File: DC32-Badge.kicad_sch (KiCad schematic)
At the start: 43 parts, among them J1 Conn_01x06, J2 Hirose_FH34-SRJ-24S, J3 Conn_01x06, J4 Conn_01x06, J5 Conn_01x06, J5 Micro_SD_Card_Det, P1 2479, Q1 RTF025N03TL, SW1 SW_Push_DPDT, SW2 EVIL_SWITCH, SW3 SW_Push, SW4 SW_Push, SW5 PROGRAM, U1 ESP32-S3-WROOM-1, U2 AP2112K-3.3

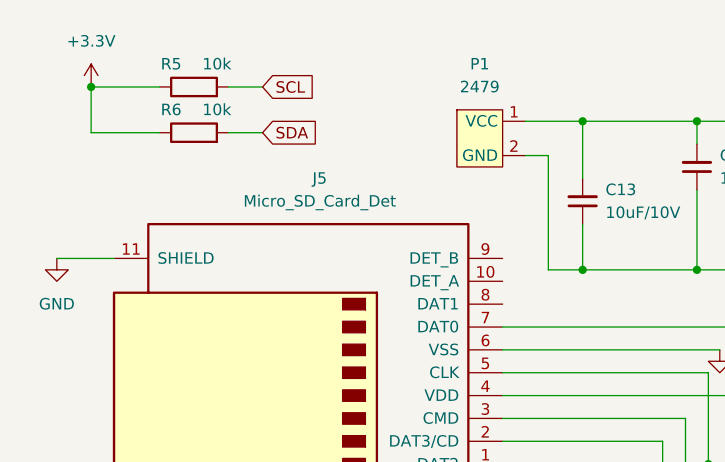
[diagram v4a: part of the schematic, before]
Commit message: Ran electrical rules checker.
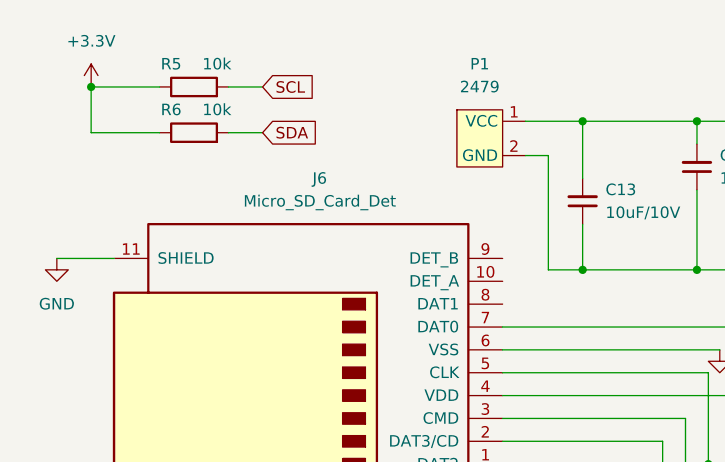
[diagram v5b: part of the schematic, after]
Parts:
- renumbered J5 to J6

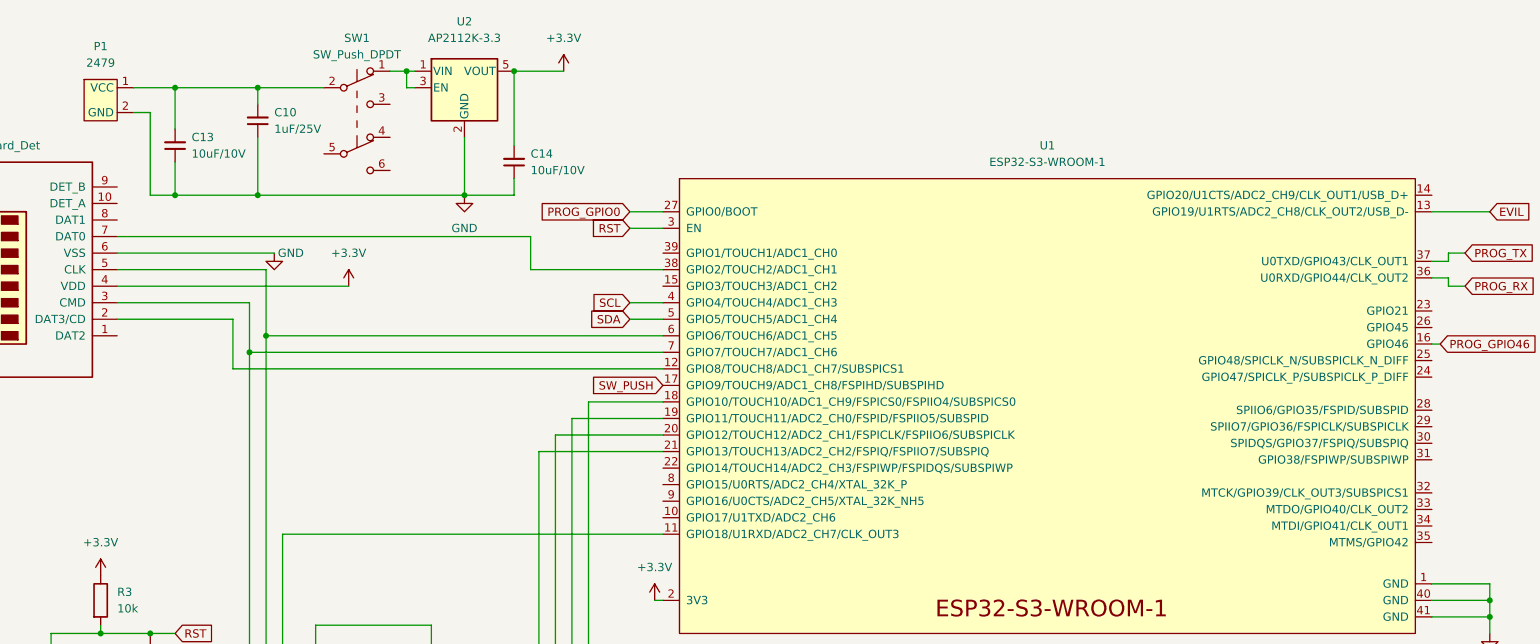
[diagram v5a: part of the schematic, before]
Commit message: Added 6 LEDs
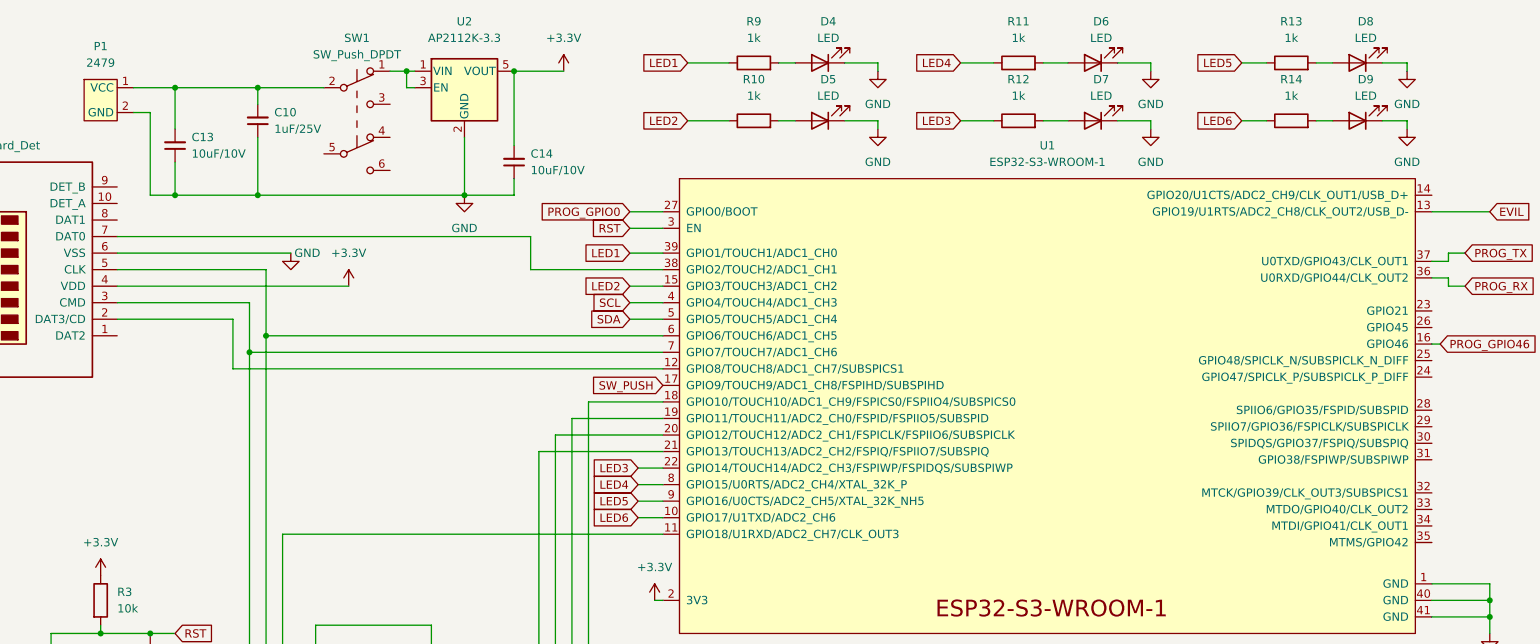
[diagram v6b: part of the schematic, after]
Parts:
- added D4, D5, D6, D7, D8, D9: LED, LED_SMD:LED_0201_0603Metric, symbol Device:LED
- added R10, R11, R12, R13, R14, R9: 1k, Resistor_SMD:R_0603_1608Metric, symbol Device:R
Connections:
- net GND: now also D4.1 (K), D5.1 (K), D6.1 (K), D7.1 (K), D8.1 (K), D9.1 (K)
- net LED6: now reaches U1.10 (GPIO17/U1TXD/ADC2_CH6)
- net LED6: now also R14.1
- net LED2: now reaches U1.15 (GPIO3/TOUCH3/ADC1_CH2)
- net LED2: now also R10.1
- net LED3: now reaches U1.22 (GPIO14/TOUCH14/ADC2_CH3/FSPIWP/FSPIDQS/SUBSPIWP)
- net LED3: now also R12.1
- net LED1: now reaches U1.39 (GPIO1/TOUCH1/ADC1_CH0)
- net LED1: now also R9.1
- net LED4: now reaches U1.8 (GPIO15/U0RTS/ADC2_CH4/XTAL_32K_P)
- net LED4: now also R11.1
- net LED5: now reaches U1.9 (GPIO16/U0CTS/ADC2_CH5/XTAL_32K_NH5)
- net LED5: now also R13.1
- new net: D8.2 (A), R13.2
- new net: D5.2 (A), R10.2
- new net: D9.2 (A), R14.2
- new net: D7.2 (A), R12.2
- new net: D6.2 (A), R11.2
- new net: D4.2 (A), R9.2

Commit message: Changed SAO board footprint to a throughhole footprint.
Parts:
- J3, J4, J5: footprint Connector_PinSocket_2.54mm:PinSocket_2x03_P2.54mm_Vertical_SMD -> Connector_PinHeader_2.54mm:PinHeader_2x03_P2.54mm_Vertical
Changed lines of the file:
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@@
       (effects (font (size 1.27 1.27)) (justify left))
     )
-    (property "Footprint" "Connector_PinSocket_2.54mm:PinSocket_2x03_P2.54mm_Vertical_SMD" (id 2) (at 205.74 116.84 0)
+    (property "Footprint" "Connector_PinHeader_2.54mm:PinHeader_2x03_P2.54mm_Vertical" (id 2) (at 205.74 116.84 0)
       (effects (font (size 1.27 1.27)) hide)
     )
@@
       (effects (font (size 1.27 1.27)) (justify left))
     )
-    (property "Footprint" "Connector_PinSocket_2.54mm:PinSocket_2x03_P2.54mm_Vertical_SMD" (id 2) (at 237.49 118.11 0)
+    (property "Footprint" "Connector_PinHeader_2.54mm:PinHeader_2x03_P2.54mm_Vertical" (id 2) (at 237.49 118.11 0)
       (effects (font (size 1.27 1.27)) hide)
     )
@@
       (effects (font (size 1.27 1.27)) (justify left))
     )
-    (property "Footprint" "Connector_PinSocket_2.54mm:PinSocket_2x03_P2.54mm_Vertical_SMD" (id 2) (at 173.99 116.84 0)
+    (property "Footprint" "Connector_PinHeader_2.54mm:PinHeader_2x03_P2.54mm_Vertical" (id 2) (at 173.99 116.84 0)
       (effects (font (size 1.27 1.27)) hide)
     )
@@
     )
     (path "/d1ba55e7-89da-4d42-b9b8-898b6fd64977"
-      (reference "J3") (unit 1) (value "Conn_01x06") (footprint "Connector_PinSocket_2.54mm:PinSocket_2x03_P2.54mm_Vertical_SMD")
+      (reference "J3") (unit 1) (value "Conn_01x06") (footprint "Connector_PinHeader_2.54mm:PinHeader_2x03_P2.54mm_Vertical")
     )
     (path "/3f83170b-e350-4ffb-9e6e-dc1ce50a1520"
-      (reference "J4") (unit 1) (value "Conn_01x06") (footprint "Connector_PinSocket_2.54mm:PinSocket_2x03_P2.54mm_Vertical_SMD")
+      (reference "J4") (unit 1) (value "Conn_01x06") (footprint "Connector_PinHeader_2.54mm:PinHeader_2x03_P2.54mm_Vertical")
     )
     (path "/fcf93aac-f8fb-4d4c-9782-4e9681b41fa9"
-      (reference "J5") (unit 1) (value "Conn_01x06") (footprint "Connector_PinSocket_2.54mm:PinSocket_2x03_P2.54mm_Vertical_SMD")
+      (reference "J5") (unit 1) (value "Conn_01x06") (footprint "Connector_PinHeader_2.54mm:PinHeader_2x03_P2.54mm_Vertical")
     )
     (path "/139aee86-9438-41b9-9b6e-0f468e21429a"

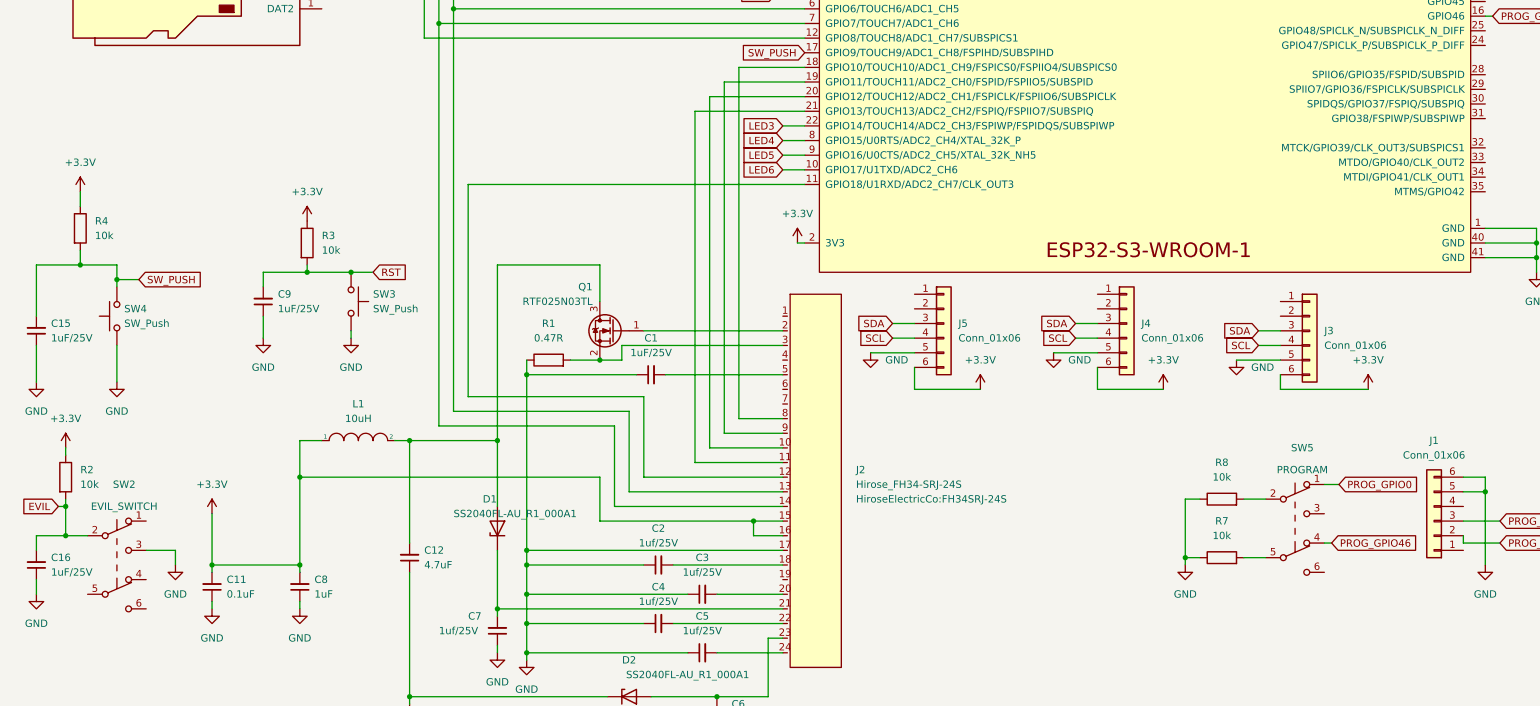
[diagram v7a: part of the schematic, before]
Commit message: Updated footprint library in schematic editor. Rearranged some componets on the PCB editor.
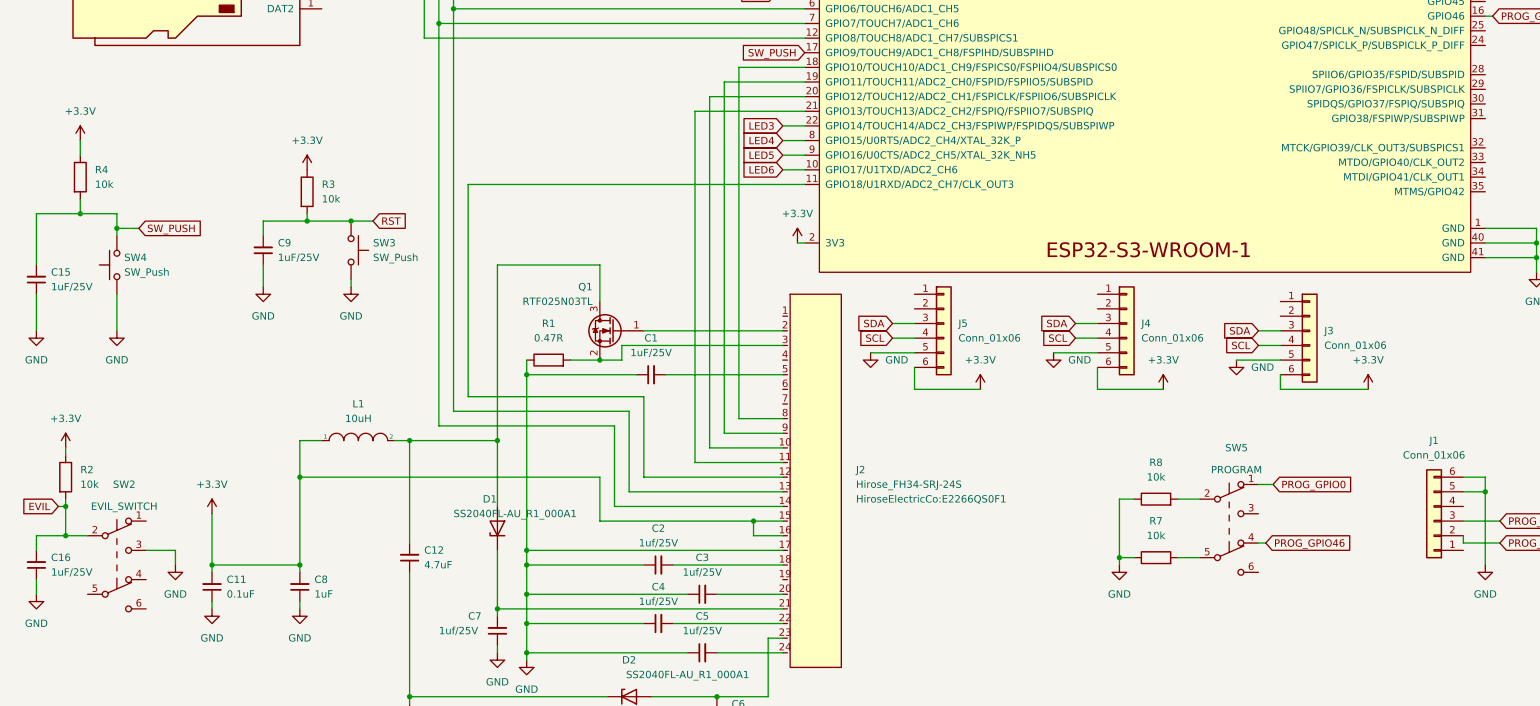
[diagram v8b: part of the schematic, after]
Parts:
- J2: footprint HiroseElectricCo:FH34SRJ-24S -> HiroseElectricCo:E2266QS0F1
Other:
- moved on the sheet: C15, C9, R3, R4, R7, R8, SW3, SW4, SW5
